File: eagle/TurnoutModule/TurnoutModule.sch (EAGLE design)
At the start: 15 parts, among them IC1 L293D, IC2 MCP23008/P

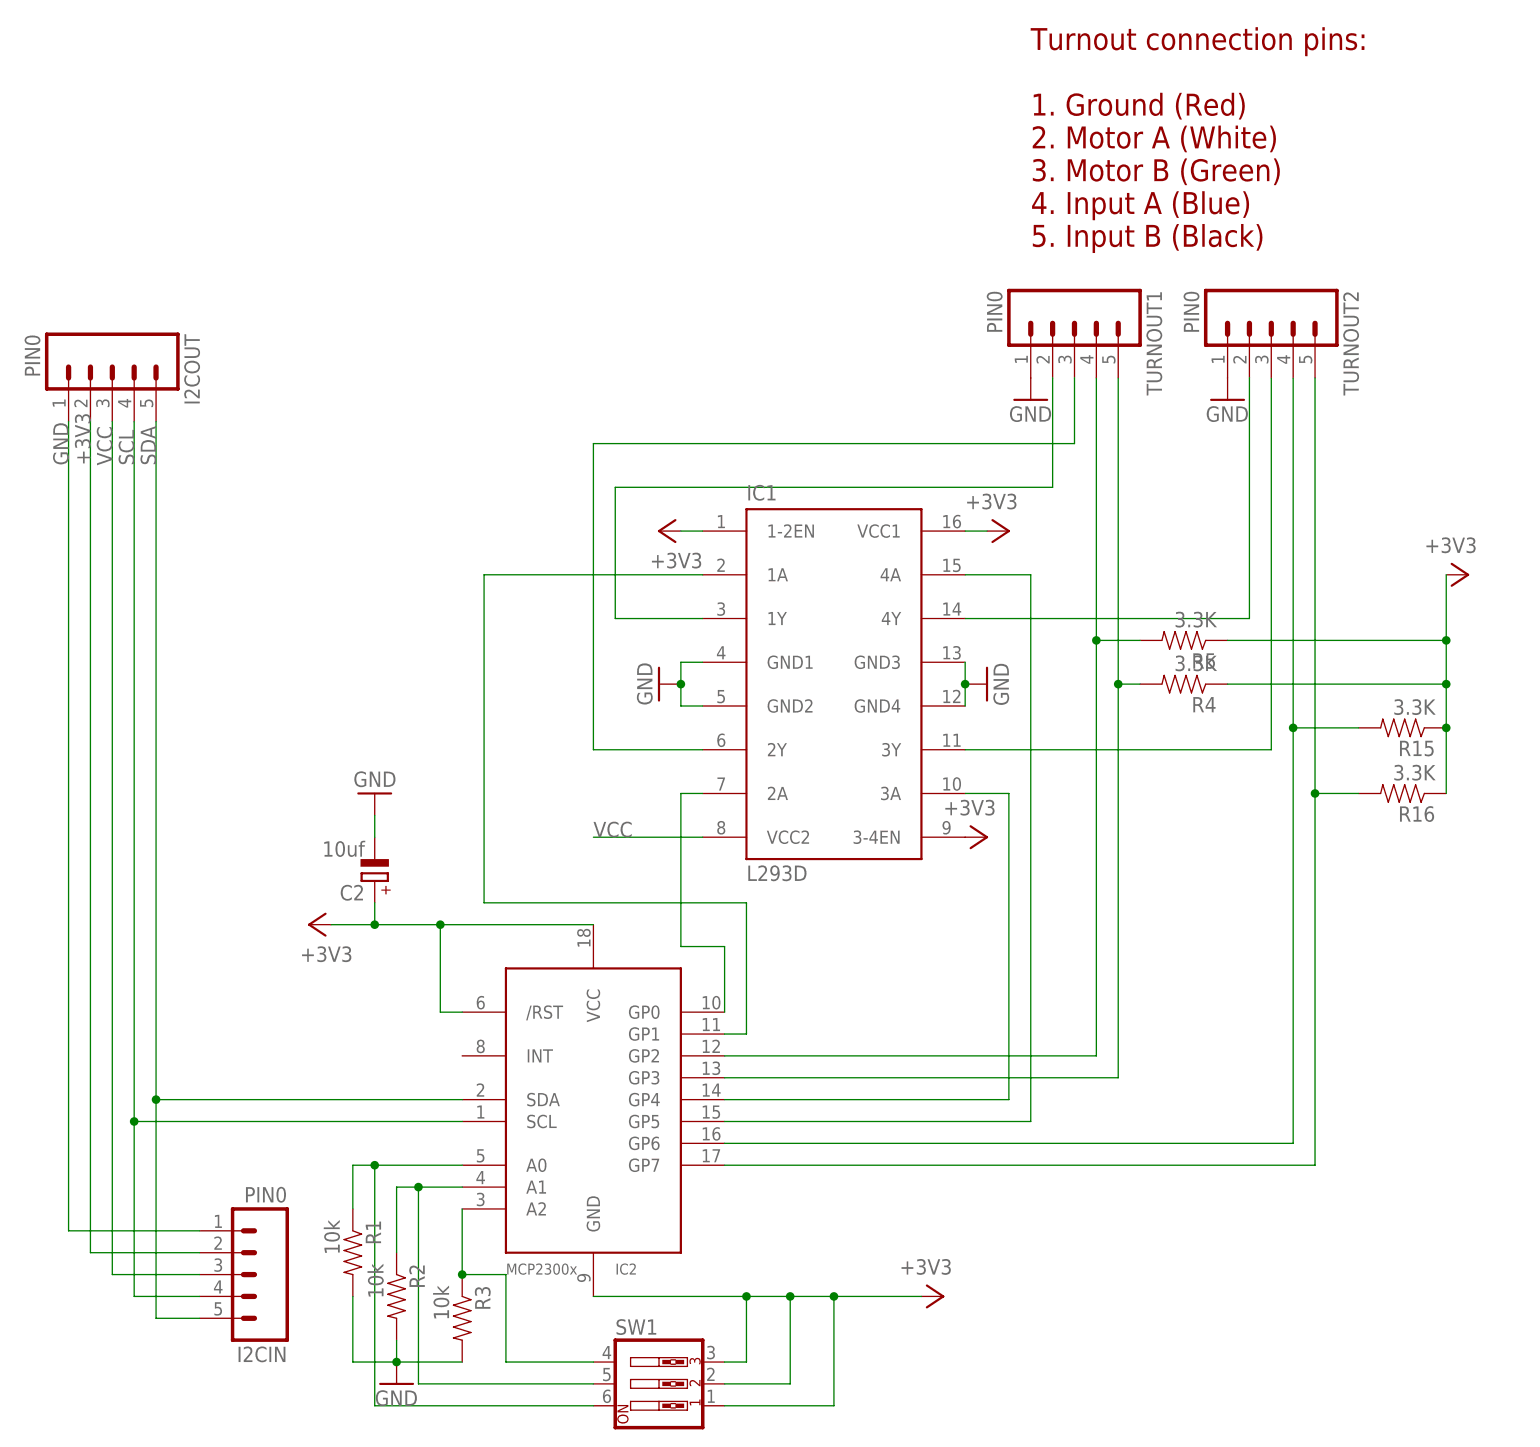
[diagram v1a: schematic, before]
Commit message: 1.  Cleanup work 2.  Reduced the retry timeout to 2 seconds (from 3) 3.  Change the TurnoutModule board to use the same address pins as the other modules 4.  Add a two-pin header to Input and Output module boards with access to GND and 3.3v 5.  Move the call to module->finishxxx to before network setup code so that the modules can initialize while the network connection is being established
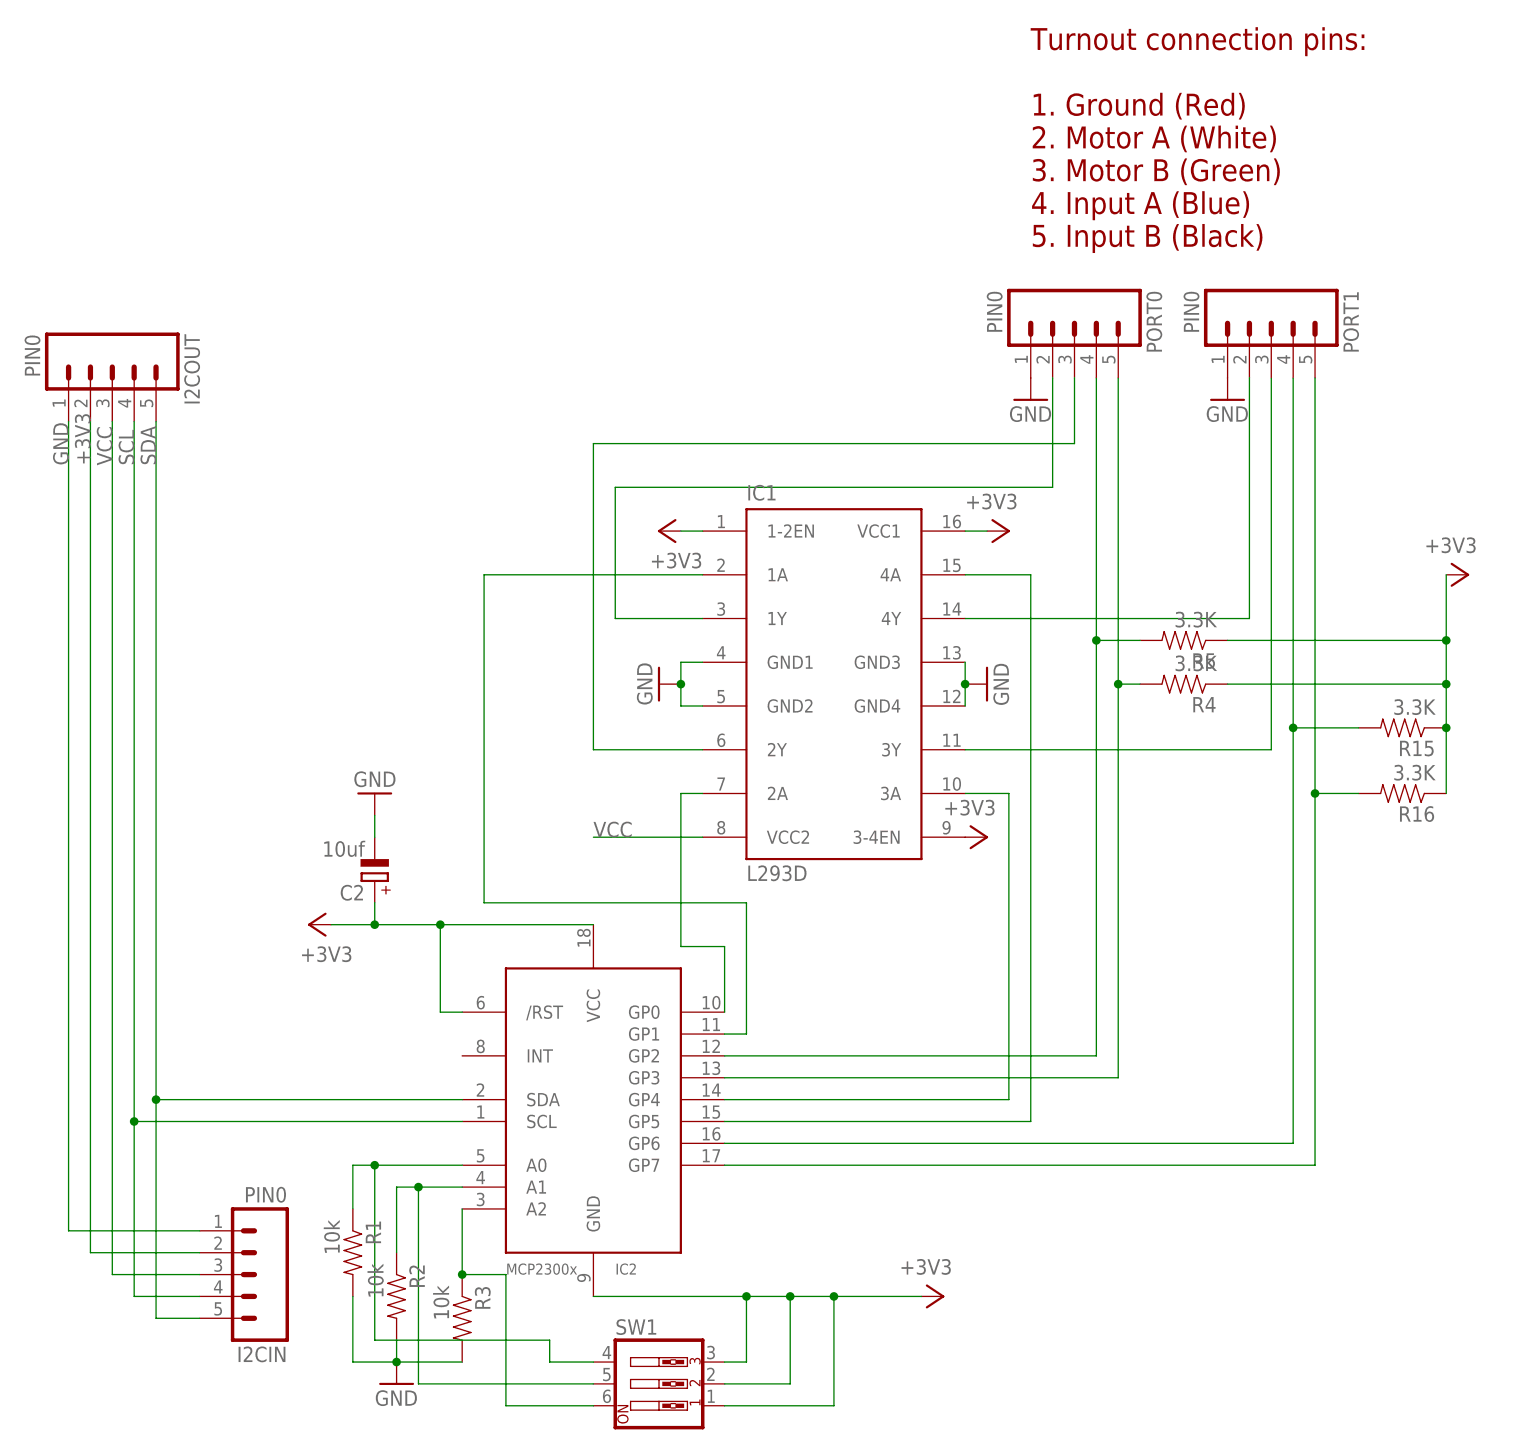
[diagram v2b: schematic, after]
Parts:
- renumbered TURNOUT1 to PORT0, TURNOUT2 to PORT1
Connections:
- net N$1: now also SW1.4; no longer SW1.6
- net N$7: now also SW1.6; no longer SW1.4
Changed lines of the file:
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@@
 </classes>
 <parts>
-<part name="TURNOUT1" library="con-amp-quick" deviceset="M05" device="" value="PIN0"/>
+<part name="PORT0" library="con-amp-quick" deviceset="M05" device="" value="PIN0"/>
 <part name="GND6" library="SparkFun-Aesthetics" deviceset="GND" device=""/>
 <part name="R15" library="SparkFun-Resistors" deviceset="RESISTOR" device="PTH-1/4W" value="3.3K"/>
 <part name="R16" library="SparkFun-Resistors" deviceset="RESISTOR" device="PTH-1/4W" value="3.3K"/>
-<part name="TURNOUT2" library="con-amp-quick" deviceset="M05" device="" value="PIN0"/>
+<part name="PORT1" library="con-amp-quick" deviceset="M05" device="" value="PIN0"/>
 <part name="IC1" library="st-microelectronics" deviceset="L293D" device=""/>
 <part name="GND12" library="SparkFun-Aesthetics" deviceset="GND" device=""/>
@@
 </plain>
 <instances>
-<instance part="TURNOUT1" gate="G$1" x="109.22" y="147.32" rot="R270"/>
+<instance part="PORT0" gate="G$1" x="109.22" y="147.32" rot="R270"/>
 <instance part="GND6" gate="1" x="104.14" y="137.16"/>
 <instance part="R15" gate="G$1" x="147.32" y="99.06" rot="R180"/>
 <instance part="R16" gate="G$1" x="147.32" y="91.44" rot="R180"/>
-<instance part="TURNOUT2" gate="G$1" x="132.08" y="147.32" rot="R270"/>
+<instance part="PORT1" gate="G$1" x="132.08" y="147.32" rot="R270"/>
 <instance part="IC1" gate="G$1" x="81.28" y="104.14"/>
 <instance part="GND12" gate="1" x="60.96" y="104.14" rot="R270"/>
@@
 <net name="GND" class="0">
 <segment>
-<pinref part="TURNOUT1" gate="G$1" pin="1"/>
+<pinref part="PORT0" gate="G$1" pin="1"/>
 <pinref part="GND6" gate="1" pin="GND"/>
 </segment>
@@
 </segment>
 <segment>
-<pinref part="TURNOUT2" gate="G$1" pin="1"/>
+<pinref part="PORT1" gate="G$1" pin="1"/>
 <pinref part="GND2" gate="1" pin="GND"/>
 </segment>
@@
 <net name="N$29" class="0">
 <segment>
-<pinref part="TURNOUT1" gate="G$1" pin="5"/>
+<pinref part="PORT0" gate="G$1" pin="5"/>
 <wire x1="114.3" y1="139.7" x2="114.3" y2="104.14" width="0.1524" layer="91"/>
 <wire x1="114.3" y1="104.14" x2="114.3" y2="58.42" width="0.1524" layer="91"/>
@@
 <segment>
 <wire x1="111.76" y1="60.96" x2="111.76" y2="109.22" width="0.1524" layer="91"/>
-<pinref part="TURNOUT1" gate="G$1" pin="4"/>
+<pinref part="PORT0" gate="G$1" pin="4"/>
 <wire x1="111.76" y1="109.22" x2="111.76" y2="139.7" width="0.1524" layer="91"/>
 <pinref part="R5" gate="G$1" pin="2"/>
@@
 <segment>
 <wire x1="137.16" y1="48.26" x2="137.16" y2="91.44" width="0.1524" layer="91"/>
-<pinref part="TURNOUT2" gate="G$1" pin="5"/>
+<pinref part="PORT1" gate="G$1" pin="5"/>
 <pinref part="R16" gate="G$1" pin="2"/>
 <wire x1="137.16" y1="91.44" x2="137.16" y2="139.7" width="0.1524" layer="91"/>
@@
 <net name="N$5" class="0">
 <segment>
-<pinref part="TURNOUT2" gate="G$1" pin="4"/>
+<pinref part="PORT1" gate="G$1" pin="4"/>
 <wire x1="134.62" y1="139.7" x2="134.62" y2="99.06" width="0.1524" layer="91"/>
 <wire x1="134.62" y1="99.06" x2="134.62" y2="50.8" width="0.1524" layer="91"/>
@@
 <segment>
 <wire x1="53.34" y1="96.52" x2="53.34" y2="132.08" width="0.1524" layer="91"/>
-<pinref part="TURNOUT1" gate="G$1" pin="3"/>
+<pinref part="PORT0" gate="G$1" pin="3"/>
 <wire x1="53.34" y1="132.08" x2="109.22" y2="132.08" width="0.1524" layer="91"/>
 <wire x1="109.22" y1="132.08" x2="109.22" y2="139.7" width="0.1524" layer="91"/>
@@
 <net name="N$10" class="0">
 <segment>
-<pinref part="TURNOUT2" gate="G$1" pin="2"/>
+<pinref part="PORT1" gate="G$1" pin="2"/>
 <wire x1="129.54" y1="111.76" x2="129.54" y2="139.7" width="0.1524" layer="91"/>
 <pinref part="IC1" gate="G$1" pin="4Y"/>
@@
 <net name="N$13" class="0">
 <segment>
-<pinref part="TURNOUT2" gate="G$1" pin="3"/>
+<pinref part="PORT1" gate="G$1" pin="3"/>
 <wire x1="132.08" y1="96.52" x2="132.08" y2="139.7" width="0.1524" layer="91"/>
 <pinref part="IC1" gate="G$1" pin="3Y"/>
@@
 <net name="N$3" class="0">
 <segment>
-<pinref part="TURNOUT1" gate="G$1" pin="2"/>
+<pinref part="PORT0" gate="G$1" pin="2"/>
 <wire x1="106.68" y1="139.7" x2="106.68" y2="127" width="0.1524" layer="91"/>
 <wire x1="106.68" y1="127" x2="55.88" y2="127" width="0.1524" layer="91"/>
@@
 <wire x1="25.4" y1="43.18" x2="25.4" y2="48.26" width="0.1524" layer="91"/>
 <wire x1="25.4" y1="48.26" x2="27.94" y2="48.26" width="0.1524" layer="91"/>
-<pinref part="SW1" gate="A" pin="6"/>
 <wire x1="27.94" y1="48.26" x2="38.1" y2="48.26" width="0.1524" layer="91"/>
-<wire x1="53.34" y1="20.32" x2="27.94" y2="20.32" width="0.1524" layer="91"/>
-<wire x1="27.94" y1="20.32" x2="27.94" y2="48.26" width="0.1524" layer="91"/>
 <junction x="27.94" y="48.26"/>
+<pinref part="SW1" gate="A" pin="4"/>
+<wire x1="27.94" y1="27.94" x2="27.94" y2="48.26" width="0.1524" layer="91"/>
+<wire x1="53.34" y1="25.4" x2="48.26" y2="25.4" width="0.1524" layer="91"/>
+<wire x1="48.26" y1="25.4" x2="48.26" y2="27.94" width="0.1524" layer="91"/>
+<wire x1="48.26" y1="27.94" x2="27.94" y2="27.94" width="0.1524" layer="91"/>
 </segment>
 </net>
@@
 <pinref part="R3" gate="G$1" pin="1"/>
 <wire x1="38.1" y1="43.18" x2="38.1" y2="35.56" width="0.1524" layer="91"/>
-<pinref part="SW1" gate="A" pin="4"/>
-<wire x1="53.34" y1="25.4" x2="43.18" y2="25.4" width="0.1524" layer="91"/>
-<wire x1="43.18" y1="25.4" x2="43.18" y2="35.56" width="0.1524" layer="91"/>
+<wire x1="43.18" y1="20.32" x2="43.18" y2="35.56" width="0.1524" layer="91"/>
 <wire x1="43.18" y1="35.56" x2="38.1" y2="35.56" width="0.1524" layer="91"/>
 <junction x="38.1" y="35.56"/>
-</segment>
-</net>
+<pinref part="SW1" gate="A" pin="6"/>
+<wire x1="53.34" y1="20.32" x2="43.18" y2="20.32" width="0.1524" layer="91"/>
+</segment>
+</net>
